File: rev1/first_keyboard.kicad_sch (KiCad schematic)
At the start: 80 parts, among them SW1 SW_Push, SW10 SW_Push, SW11 SW_Push, SW12 SW_Push, SW13 SW_Push, SW14 SW_Push, SW15 SW_Push, SW16 SW_Push, SW17 SW_Push, SW18 SW_Push, SW19 SW_Push, SW2 SW_Push, SW20 SW_Push, SW21 SW_Push, SW22 SW_Push, SW23 SW_Push, SW24 SW_Push, SW25 SW_Push, SW26 SW_Push, SW27 SW_Push, SW28 SW_Push, SW29 SW_Push, SW3 SW_Push, SW30 SW_Push, SW31 SW_Push, SW32 SW_Push, SW33 SW_Push, SW34 SW_Push, SW35 SW_Push, SW36 SW_Push, SW37 SW_Push, SW38 SW_Push, SW39 SW_Push, SW4 SW_Push, SW40 SW_Push, SW5 SW_Push, SW6 SW_Push, SW7 SW_Push, SW8 SW_Push, SW9 SW_Push, U1 Pico

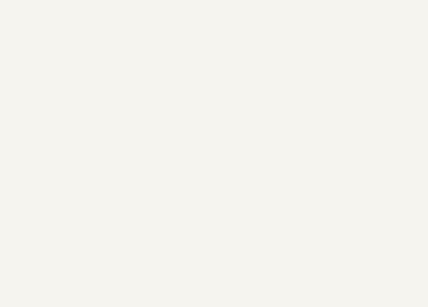
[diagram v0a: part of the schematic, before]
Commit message: fix: ねじ穴に変更
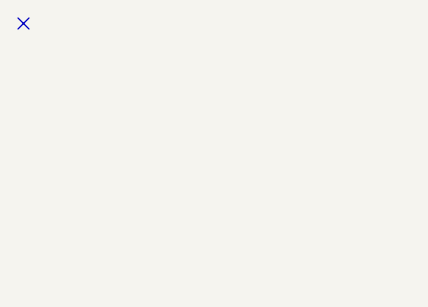
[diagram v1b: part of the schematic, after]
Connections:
- no-connect marks 18 -> 19
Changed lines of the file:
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@@
   (no_connect (at 83.82 187.96))
   (no_connect (at 119.38 195.58))
+  (no_connect (at -83.82 110.49))
   (no_connect (at 83.82 175.26))
   (no_connect (at 83.82 180.34))

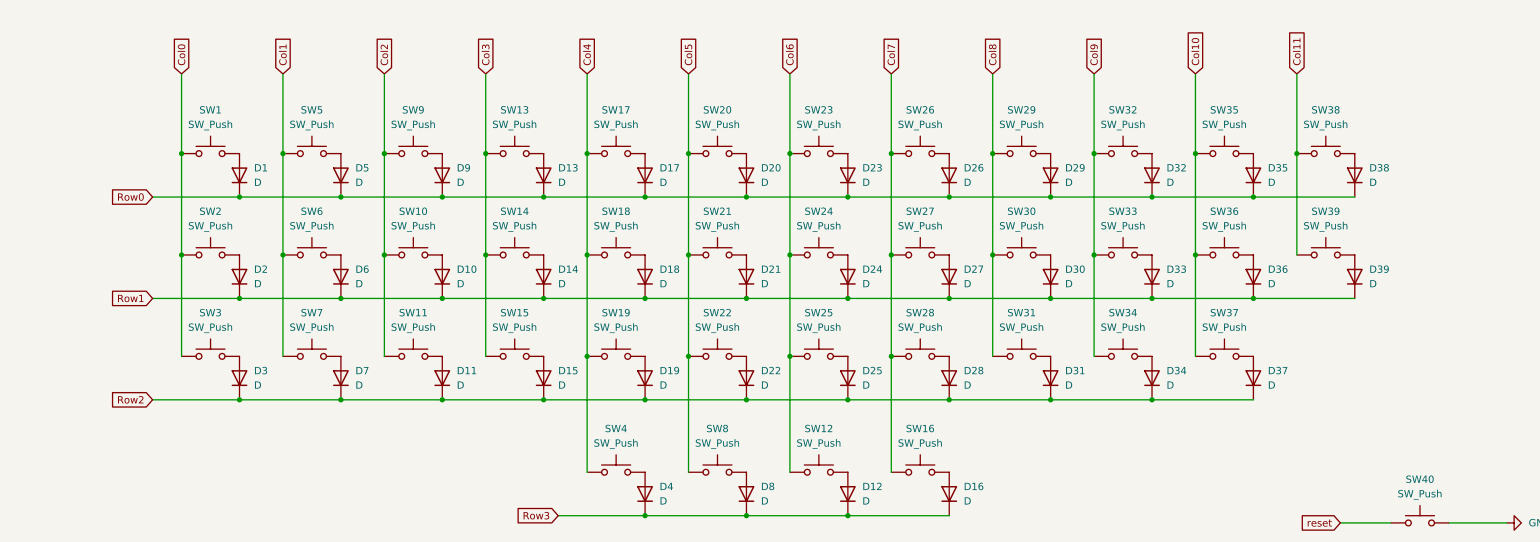
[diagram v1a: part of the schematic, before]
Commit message: feat: 回路図にスイッチを追加
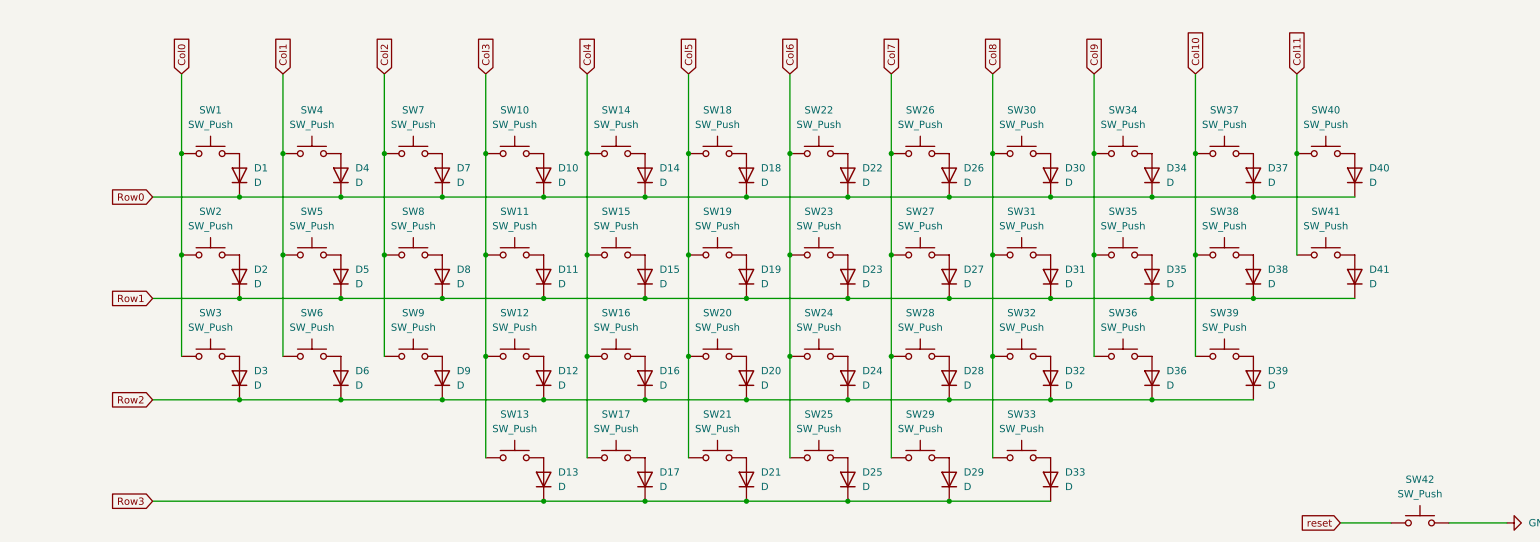
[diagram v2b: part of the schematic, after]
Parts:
- added D13, D33: D, kbd_Parts:Diode_TH_SMD, symbol Device:D
- added SW13, SW33: SW_Push, kbd_SW:CherryMX_Hotswap_1u, symbol Switch:SW_Push
- renumbered D13 to D10, D14 to D11, D15 to D12, D17 to D14, D18 to D15, D19 to D16, D4 to D17, D20 to D18, D21 to D19, D22 to D20, D8 to D21, D23 to D22, D24 to D23, D25 to D24, D12 to D25, D16 to D29, D29 to D30, D30 to D31, D31 to D32, D32 to D34, D33 to D35, D34 to D36, D35 to D37, D36 to D38, D37 to D39, D5 to D4, D38 to D40, D39 to D41, D6 to D5, D7 to D6, D9 to D7, D10 to D8, D11 to D9, SW13 to SW10, SW14 to SW11, SW15 to SW12, SW17 to SW14, SW18 to SW15, SW19 to SW16, SW4 to SW17, SW20 to SW18, SW21 to SW19, SW22 to SW20, SW8 to SW21, SW23 to SW22, SW24 to SW23, SW25 to SW24, SW12 to SW25, SW16 to SW29, SW29 to SW30, SW30 to SW31, SW31 to SW32, SW32 to SW34, SW33 to SW35, SW34 to SW36, SW35 to SW37, SW36 to SW38, SW37 to SW39, SW5 to SW4, SW38 to SW40, SW39 to SW41, SW40 to SW42, SW6 to SW5, SW7 to SW6, SW9 to SW7, SW10 to SW8, SW11 to SW9
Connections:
- net Col3: now also SW13.1
- net Col8: now also SW33.1
- net Row3: now also D13.1 (K), D33.1 (K)
- new net: D13.2 (A), SW13.2
- new net: D33.2 (A), SW33.2
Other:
- moved on the sheet: D17, D21, D25, D29, SW17, SW21, SW25, SW29

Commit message: feat: 回路図をpicoがスイッチと同じ面に来る想定のものに変更
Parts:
- removed SW42: SW_Push, kbd_Parts:ResetSW, symbol Switch:SW_Push
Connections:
- net Col0: now also U1.14 (GPIO10); no longer U1.22 (GPIO17)
- net Col1: now also U1.15 (GPIO11); no longer U1.21 (GPIO16)
- net Col10: now also U1.22 (GPIO17); no longer U1.10 (GPIO7)
- net Col11: now also U1.21 (GPIO16); no longer U1.9 (GPIO6)
- net Col2: now also U1.16 (GPIO12); no longer U1.20 (GPIO15)
- net Col3: now also U1.17 (GPIO13); no longer U1.19 (GPIO14)
- net Col4: now also U1.19 (GPIO14); no longer U1.17 (GPIO13)
- net Col5: now also U1.20 (GPIO15); no longer U1.16 (GPIO12)
- net Col6: now also U1.27 (GPIO21); no longer U1.15 (GPIO11)
- net Col7: now also U1.26 (GPIO20); no longer U1.14 (GPIO10)
- net Col8: now also U1.25 (GPIO19); no longer U1.12 (GPIO9)
- net Col9: now also U1.24 (GPIO18); no longer U1.11 (GPIO8)
- net GND: now also U1.40 (VBUS)
- net Row0: now also U1.9 (GPIO6); no longer U1.27 (GPIO21)
- net Row1: now also U1.10 (GPIO7); no longer U1.26 (GPIO20)
- net Row2: now also U1.11 (GPIO8); no longer U1.25 (GPIO19)
- net Row3: now also U1.12 (GPIO9); no longer U1.24 (GPIO18)
- net reset: no longer names the net of U1.30 (RUN)
- no-connect marks 19 -> 20

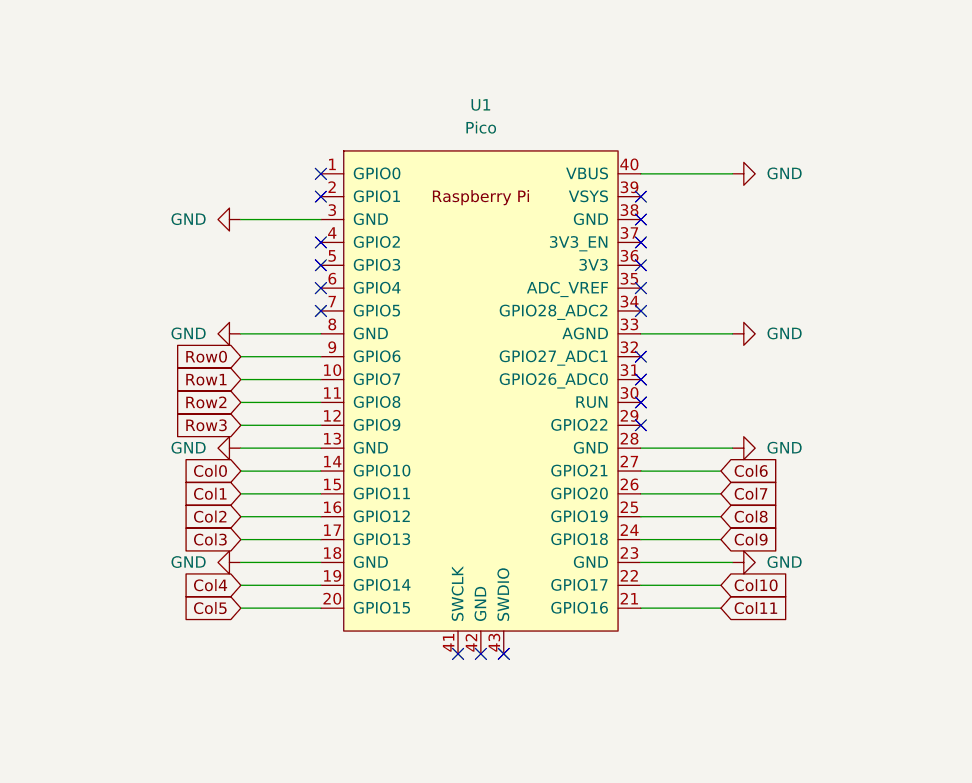
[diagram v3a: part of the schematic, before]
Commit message: feat: 小指カラムをさげる part1
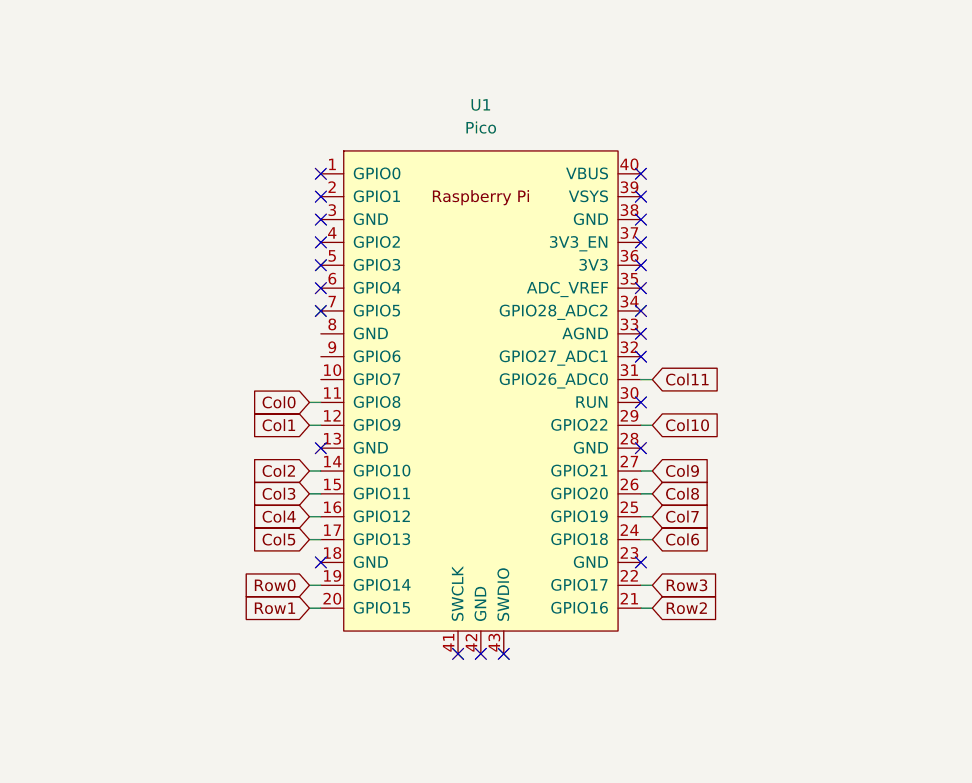
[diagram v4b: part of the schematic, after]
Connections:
- net Col0: now also U1.11 (GPIO8); no longer U1.14 (GPIO10)
- net Col1: now also U1.12 (GPIO9); no longer U1.15 (GPIO11)
- net Col10: now also U1.29 (GPIO22); no longer U1.22 (GPIO17)
- net Col11: now also U1.31 (GPIO26_ADC0); no longer U1.21 (GPIO16)
- net Col2: now also U1.14 (GPIO10); no longer U1.16 (GPIO12)
- net Col3: now also U1.15 (GPIO11); no longer U1.17 (GPIO13)
- net Col4: now also U1.16 (GPIO12); no longer U1.19 (GPIO14)
- net Col5: now also U1.17 (GPIO13); no longer U1.20 (GPIO15)
- net Col6: now also U1.24 (GPIO18); no longer U1.27 (GPIO21)
- net Col7: now also U1.25 (GPIO19); no longer U1.26 (GPIO20)
- net Col8: now also U1.26 (GPIO20); no longer U1.25 (GPIO19)
- net Col9: now also U1.27 (GPIO21); no longer U1.24 (GPIO18)
- net Row0: now also U1.19 (GPIO14); no longer U1.9 (GPIO6)
- net Row1: now also U1.20 (GPIO15); no longer U1.10 (GPIO7)
- net Row2: now also U1.21 (GPIO16); no longer U1.11 (GPIO8)
- net Row3: now also U1.22 (GPIO17); no longer U1.12 (GPIO9)
- removed net GND: U1.13 (GND), U1.18 (GND), U1.23 (GND), U1.28 (GND), U1.3 (GND), U1.33 (AGND), U1.40 (VBUS), U1.8 (GND)
- no-connect marks 20 -> 25
